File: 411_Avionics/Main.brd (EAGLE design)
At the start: 45.4 x 57.1 mm, 25 parts, among them CN1 Battery Connector, IC1 BQ24022, IC3 74AC11138D, T1 NTR1P02, T2 NTR1P02, U1 USB_In, U2 ATTINY85V-10SU, U3 LSM9DS0, U5 LM317DCY

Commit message: Schematic reorganized and touched up
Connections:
- removed net MEM: U$1.1
- removed net N$3: U2.2
- removed net N$5: U3.19
- removed net N$6: U2.3
- removed net N$7: U2.1
- removed net N$8: U3.20
- new net GYR_EN: IC3.14, U3.19
- new net MEM_EN: IC3.15, U$1.1
- new net SEL0: IC3.1, U2.2
- new net SEL1: IC3.2, U2.3
- new net SEL2: IC3.3, U2.1
- new net XM_EN: IC3.13, U3.20
- net GND: now also C9.1, IC3.5, IC3.6, IC3.8; no longer C9.2
- net N$17: now also C1.1, C8.1, IC1.10, U5.3
- net N$18: no longer C1.1, C8.1, IC1.10, U5.3
- net VCC: now also C9.2, IC3.16, IC3.4; no longer C9.1
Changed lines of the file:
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@@
 <contactref element="U1" pad="GND1"/>
 <contactref element="R1" pad="1"/>
-<contactref element="U2" pad="4"/>
 <contactref element="U3" pad="2"/>
 <contactref element="U3" pad="3"/>
@@
 <contactref element="C1" pad="2"/>
 <contactref element="C8" pad="2"/>
-<contactref element="C9" pad="2"/>
 <contactref element="R5" pad="1"/>
+<contactref element="IC3" pad="8"/>
+<contactref element="IC3" pad="5"/>
+<contactref element="IC3" pad="6"/>
+<contactref element="U2" pad="4"/>
+<contactref element="C9" pad="1"/>
 <wire x1="29.53" y1="44.45" x2="36.51" y2="52.07" width="0" layer="19" extent="1-1"/>
 <wire x1="25.08" y1="44.45" x2="29.53" y2="44.45" width="0" layer="19" extent="1-1"/>
@@
 <wire x1="17.78" y1="30.685" x2="18.28" y2="30.685" width="0" layer="19" extent="1-1"/>
 <wire x1="17.28" y1="30.685" x2="17.78" y2="30.685" width="0" layer="19" extent="1-1"/>
-<wire x1="16.51" y1="36.83" x2="17.28" y2="30.685" width="0" layer="19" extent="1-1"/>
+<wire x1="11.43" y1="36.83" x2="17.28" y2="30.685" width="0" layer="19" extent="1-1"/>
+<wire x1="7.94" y1="44.45" x2="11.43" y2="36.83" width="0" layer="19" extent="1-1"/>
+<wire x1="2.86" y1="44.45" x2="7.94" y2="44.45" width="0" layer="19" extent="1-1"/>
+<wire x1="1.6002" y1="36.576" x2="2.86" y2="44.45" width="0" layer="19" extent="1-1"/>
+<wire x1="13.97" y1="50.8" x2="7.94" y2="44.45" width="0" layer="19" extent="1-1"/>
 <wire x1="34.29" y1="36.83" x2="25.4" y2="36.83" width="0" layer="19" extent="1-1"/>
 <wire x1="43.18" y1="36.83" x2="34.29" y2="36.83" width="0" layer="19" extent="1-1"/>
 <wire x1="20.16" y1="17.145" x2="24.795" y2="26.69" width="0" layer="19" extent="1-1"/>
-<wire x1="7.94" y1="44.45" x2="16.51" y2="36.83" width="0" layer="19" extent="1-1"/>
-<wire x1="2.86" y1="44.45" x2="7.94" y2="44.45" width="0" layer="19" extent="1-1"/>
-<wire x1="1.6002" y1="36.576" x2="2.86" y2="44.45" width="0" layer="19" extent="1-1"/>
-<wire x1="13.97" y1="50.8" x2="7.94" y2="44.45" width="0" layer="19" extent="1-1"/>
 <wire x1="20.4216" y1="3.175" x2="20.16" y2="17.145" width="0" layer="19" extent="1-1"/>
 <wire x1="43.34" y1="16.48" x2="43.18" y2="36.83" width="0" layer="19" extent="1-1"/>
+<wire x1="-1.905" y1="3.2766" x2="20.4216" y2="3.175" width="0" layer="19" extent="1-1"/>
+<wire x1="-4.445" y1="3.2766" x2="-1.905" y2="3.2766" width="0" layer="19" extent="1-1"/>
+<wire x1="-5.715" y1="3.2766" x2="-4.445" y2="3.2766" width="0" layer="19" extent="1-1"/>
 </signal>
 <signal name="N$4">
@@
 </signal>
 <signal name="CLK">
-<contactref element="U2" pad="7"/>
 <contactref element="U$1" pad="6"/>
 <contactref element="U3" pad="21"/>
-<wire x1="25.56" y1="18.415" x2="27.8384" y2="5.715" width="0" layer="19" extent="1-1"/>
-<wire x1="26.92" y1="29.815" x2="25.56" y2="18.415" width="0" layer="19" extent="1-1"/>
+<contactref element="U2" pad="7"/>
+<wire x1="25.56" y1="18.415" x2="26.92" y2="29.815" width="0" layer="19" extent="1-1"/>
+<wire x1="27.8384" y1="5.715" x2="25.56" y2="18.415" width="0" layer="19" extent="1-1"/>
 </signal>
 <signal name="MISO">
@@
 <wire x1="25.42" y1="29.815" x2="25.56" y2="17.145" width="0" layer="19" extent="1-1"/>
 </signal>
-<signal name="N$3">
-<contactref element="U2" pad="2"/>
-</signal>
-<signal name="N$6">
-<contactref element="U2" pad="3"/>
-</signal>
-<signal name="N$7">
-<contactref element="U2" pad="1"/>
-</signal>
-<signal name="MEM">
+<signal name="MEM_EN">
 <contactref element="U$1" pad="1"/>
-</signal>
-<signal name="N$8">
+<contactref element="IC3" pad="15"/>
+<wire x1="-9.525" y1="9.4234" x2="20.16" y2="20.955" width="0" layer="19" extent="1-1"/>
+</signal>
+<signal name="XM_EN">
 <contactref element="U3" pad="20"/>
+<contactref element="IC3" pad="13"/>
+<wire x1="-6.985" y1="9.4234" x2="27.42" y2="29.815" width="0" layer="19" extent="1-1"/>
 </signal>
 <signal name="N$9">
@@
 <contactref element="U$1" pad="7"/>
 <contactref element="U$1" pad="3"/>
+<contactref element="IC3" pad="16"/>
+<contactref element="IC3" pad="4"/>
+<contactref element="U2" pad="8"/>
+<contactref element="C9" pad="2"/>
 <contactref element="U5" pad="4"/>
+<contactref element="R4" pad="2"/>
 <contactref element="U5" pad="2"/>
-<contactref element="R4" pad="2"/>
-<contactref element="C9" pad="1"/>
-<contactref element="U2" pad="8"/>
 <wire x1="23.18" y1="44.45" x2="34.61" y2="52.07" width="0" layer="19" extent="1-1"/>
 <wire x1="14.92" y1="44.45" x2="23.18" y2="44.45" width="0" layer="19" extent="1-1"/>
-<wire x1="11.43" y1="36.83" x2="14.92" y2="44.45" width="0" layer="19" extent="1-1"/>
-<wire x1="28.545" y1="29.19" x2="23.18" y2="44.45" width="0" layer="19" extent="1-1"/>
+<wire x1="16.51" y1="36.83" x2="14.92" y2="44.45" width="0" layer="19" extent="1-1"/>
+<wire x1="28.545" y1="29.19" x2="16.51" y2="36.83" width="0" layer="19" extent="1-1"/>
 <wire x1="28.545" y1="28.69" x2="28.545" y2="29.19" width="0" layer="19" extent="1-1"/>
 <wire x1="28.545" y1="28.19" x2="28.545" y2="28.69" width="0" layer="19" extent="1-1"/>
@@
 <wire x1="12.0904" y1="6.35" x2="20.16" y2="18.415" width="0" layer="19" extent="1-1"/>
 <wire x1="5.6896" y1="6.35" x2="12.0904" y2="6.35" width="0" layer="19" extent="1-1"/>
-</signal>
-<signal name="N$5">
+<wire x1="-6.985" y1="3.2766" x2="5.6896" y2="6.35" width="0" layer="19" extent="1-1"/>
+<wire x1="-10.795" y1="9.4234" x2="-6.985" y2="3.2766" width="0" layer="19" extent="1-1"/>
+</signal>
+<signal name="GYR_EN">
 <contactref element="U3" pad="19"/>
+<contactref element="IC3" pad="14"/>
+<wire x1="-8.255" y1="9.4234" x2="27.92" y2="29.815" width="0" layer="19" extent="1-1"/>
 </signal>
 <signal name="N$12">
@@
 <contactref element="U$2" pad="6"/>
 <contactref element="R2" pad="2"/>
-<wire x1="9.21" y1="30.61" x2="31.43" y2="44.45" width="0" layer="19" extent="1-1"/>
-</signal>
-<signal name="N$18">
 <contactref element="C1" pad="1"/>
 <contactref element="IC1" pad="10"/>
+<contactref element="U5" pad="3"/>
+<contactref element="C8" pad="1"/>
+<wire x1="38.1" y1="36.83" x2="31.43" y2="44.45" width="0" layer="19" extent="1-1"/>
+<wire x1="20.32" y1="36.83" x2="31.43" y2="44.45" width="0" layer="19" extent="1-1"/>
+<wire x1="16.78" y1="30.685" x2="20.32" y2="36.83" width="0" layer="19" extent="1-1"/>
+<wire x1="9.21" y1="30.61" x2="16.78" y2="30.685" width="0" layer="19" extent="1-1"/>
+<wire x1="5.6896" y1="4.0386" x2="9.21" y2="30.61" width="0" layer="19" extent="1-1"/>
+</signal>
+<signal name="N$18">
 <contactref element="R3" pad="2"/>
 <contactref element="CN1" pad="1"/>
-<contactref element="U5" pad="3"/>
-<contactref element="C8" pad="1"/>
-<wire x1="10.7" y1="16.35" x2="5.6896" y2="4.0386" width="0" layer="19" extent="1-1"/>
-<wire x1="16.78" y1="30.685" x2="10.7" y2="16.35" width="0" layer="19" extent="1-1"/>
-<wire x1="20.32" y1="36.83" x2="16.78" y2="30.685" width="0" layer="19" extent="1-1"/>
-<wire x1="20" y1="44.45" x2="20.32" y2="36.83" width="0" layer="19" extent="1-1"/>
-<wire x1="38.1" y1="36.83" x2="20.32" y2="36.83" width="0" layer="19" extent="1-1"/>
+<wire x1="10.7" y1="16.35" x2="20" y2="44.45" width="0" layer="19" extent="1-1"/>
 </signal>
 <signal name="N$20">
-<contactref element="U5" pad="1"/>
 <contactref element="R5" pad="2"/>
 <contactref element="R4" pad="1"/>
-<wire x1="9.84" y1="44.45" x2="5.6896" y2="8.6614" width="0" layer="19" extent="1-1"/>
-<wire x1="13.02" y1="44.45" x2="9.84" y2="44.45" width="0" layer="19" extent="1-1"/>
+<contactref element="U5" pad="1"/>
+<wire x1="9.84" y1="44.45" x2="13.02" y2="44.45" width="0" layer="19" extent="1-1"/>
+<wire x1="5.6896" y1="8.6614" x2="9.84" y2="44.45" width="0" layer="19" extent="1-1"/>
 </signal>
 <signal name="N$1">
@@
 <wire x1="43.34" y1="19.08" x2="29.21" y2="36.83" width="0" layer="19" extent="1-1"/>
 </signal>
+<signal name="SEL0">
+<contactref element="U2" pad="2"/>
+<contactref element="IC3" pad="1"/>
+<wire x1="-10.795" y1="3.2766" x2="20.4216" y2="5.715" width="0" layer="19" extent="1-1"/>
+</signal>
+<signal name="SEL1">
+<contactref element="U2" pad="3"/>
+<contactref element="IC3" pad="2"/>
+<wire x1="-9.525" y1="3.2766" x2="20.4216" y2="4.445" width="0" layer="19" extent="1-1"/>
+</signal>
+<signal name="SEL2">
+<contactref element="U2" pad="1"/>
+<contactref element="IC3" pad="3"/>
+<wire x1="-8.255" y1="3.2766" x2="20.4216" y2="6.985" width="0" layer="19" extent="1-1"/>
+</signal>
 </signals>

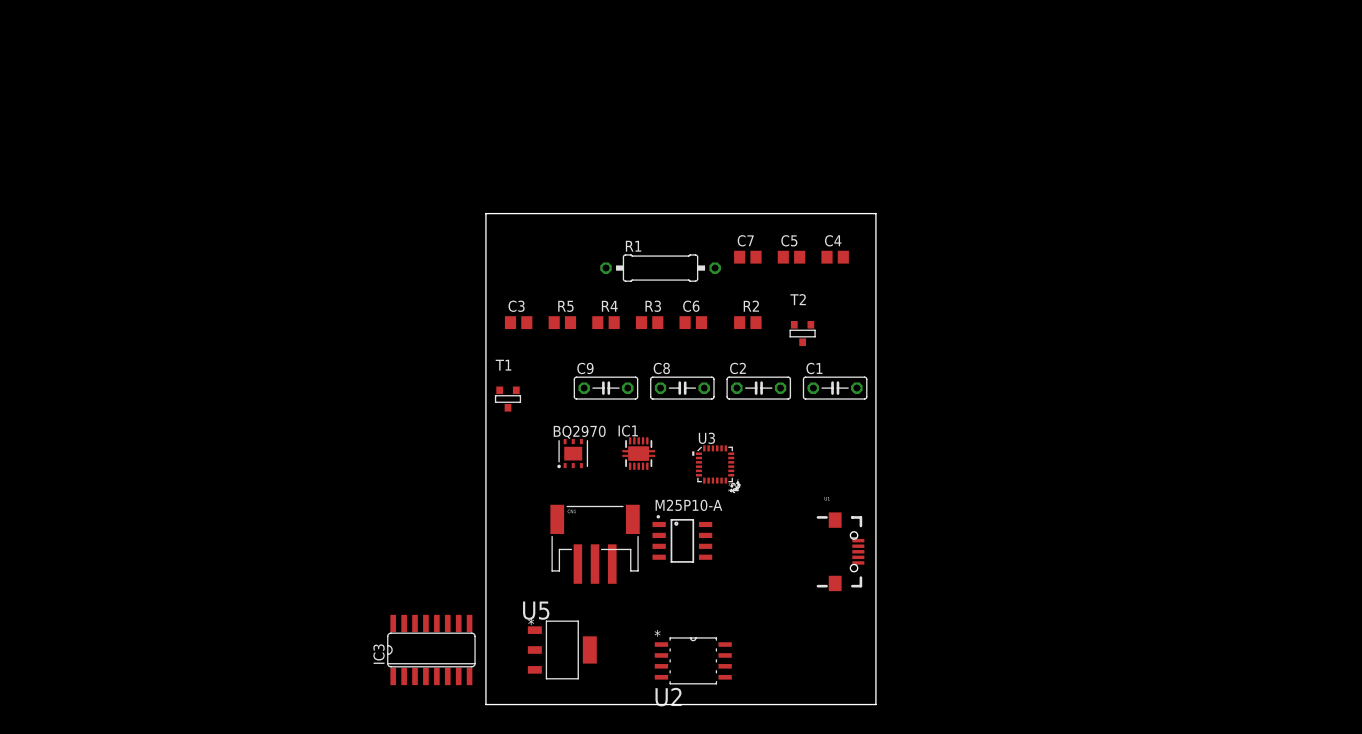
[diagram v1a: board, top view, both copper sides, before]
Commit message: Re-made Main.brd file to reflect most recent schematic.
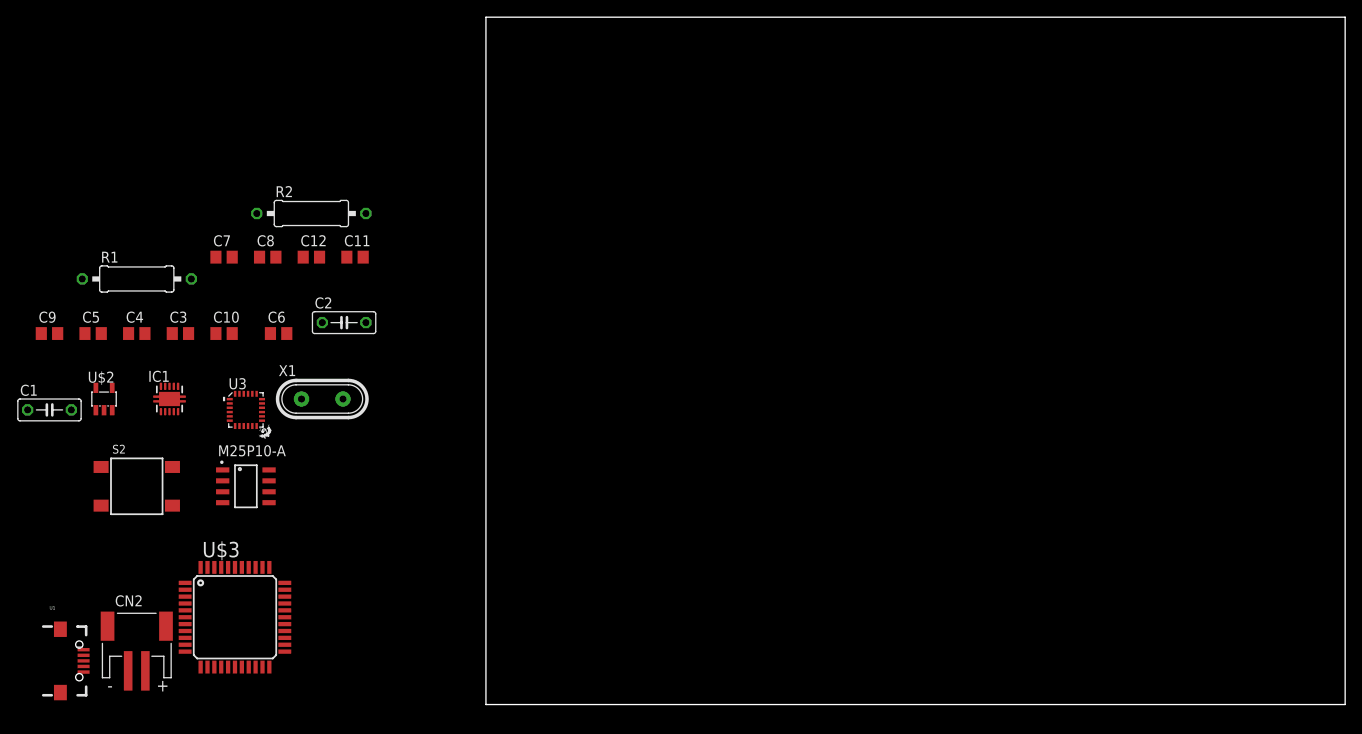
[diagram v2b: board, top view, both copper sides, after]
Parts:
- removed CN1: Battery Connector, adafruit:JSTPH3
- removed IC3: 74AC11138D, 74ac-logic:SO16
- removed R3: 330, resistor:R0805
- removed R4: 240, resistor:R0805
- removed R5: 390, resistor:R0805
- removed T1, T2: NTR1P02, zetex:SOT-23
- removed U2: ATTINY85V-10SU, ATTINY85V-10SU:SOIC127P798X216-8N
- removed U5: LM317DCY, LM317DCY:SOT230P700X180-4N
- added C10: 100n, rcl:C0805
- added C11, C12: 22p, rcl:C0805
- added CN2: (no value), adafruit:JST-PH-2-SMT-RA
- added S2: PTS645SM43SMTR92, switch-ck:PTS645-SMD
- added U$3: ATMEGA32U4-AU, adafruit:TQFP44
- added X1: 8MHz, IQD-Frequency-Products:HC49
- C7: value .1µ -> 1µ
- C8: value 2.2µ -> 10u; device rcl:C050-025X075 -> rcl:C0805
- C9: device rcl:C050-025X075 -> rcl:C0805
- R2: value 2.2k -> 10k; device resistor:R0805 -> rcl:0309/12
- U$2: value BQ2970 -> LP5907; device WSON-6-PAD:WSON-6-PAD -> adafruit:SOT23-5L
- moved C1 91.5 mm to (-50.8, 34.3)
- moved U1 91.1 mm to (-49.5, 5.08)
- moved C4 81.8 mm to (-40.6, 43.2)
- moved C5 81.8 mm to (-45.7, 43.2)
- moved C9 65.1 mm to (-50.8, 43.2)
- moved R1 61.0 mm to (-40.6, 49.5)
- moved C7 61.0 mm to (-30.5, 52.1)
- moved IC1 55.0 mm to (-36.8, 35.6)
- moved U$2 55.0 mm to (-44.5, 35.6)
- moved U3 55.0 mm to (-27.9, 34.3)
- moved R2 52.4 mm to (-20.3, 57.1)
- moved U$1 51.2 mm to (-27.9, 25.4)
- moved C8 50.6 mm to (-25.4, 52.1)
- moved C2 48.9 mm to (-16.5, 44.5)
- moved C6 48.3 mm to (-24.1, 43.2)
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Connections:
- removed net N$12: T1.3, U$2.2
- removed net N$13: T2.3, U$2.3
- removed net N$14: T1.1, T2.1
- removed net N$15: C7.1, R3.1, U$2.5
- removed net N$16: C7.2, CN1.2, T2.2, U$2.4
- removed net N$18: CN1.1, R3.2
- removed net N$20: R4.1, R5.2, U5.1
- removed net SEL0: IC3.1, U2.2
- removed net SEL1: IC3.2, U2.3
- removed net SEL2: IC3.3, U2.1
- new net D+: U$3.4, U1.D+1
- new net D-: U$3.3, U1.D-1
- new net N$2: C11.1, U$3.17, X1.1
- new net N$3: R2.2, S2.3, S2.4, U$3.13
- new net N$5: C12.1, U$3.16, X1.2
- new net N$6: C8.1, S2.1, S2.2
- new net VBUS1: U$3.7
- net CLK: now also U$3.9; no longer U2.7
- net GND: now also C10.2, C11.2, C12.2, C7.2, C9.2, CN2.2, U$2.2, U$3.15, U$3.23, U$3.33, U$3.35, U$3.43, U$3.5; no longer C9.1, IC3.5, IC3.6, IC3.8, R2.1, R5.1, T1.2, U2.4
- net GYR_EN: now also U$3.38; no longer IC3.14
- net MEM_EN: now also U$3.40; no longer IC3.15
- net MISO: now also U$3.11; no longer U2.6
- net MOSI: now also U$3.10; no longer U2.5
- net N$17: now also CN2.1, U$2.1, U$2.3; no longer C8.1, R2.2, U$2.6, U5.3
- net VCC: now also C10.1, C7.1, C9.1, R2.1, U$2.5, U$3.14, U$3.24, U$3.34, U$3.44, U$3.6; no longer C9.2, IC3.16, IC3.4, R4.2, U2.8, U5.2, U5.4
- net XM_EN: now also U$3.39; no longer IC3.13
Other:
- board size 45.4 x 57.1 mm -> 100 x 80 mm
